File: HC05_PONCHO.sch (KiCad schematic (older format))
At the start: 15 parts

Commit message: Actualizacion de esquematico
-Esquematico graficamente completo.
-Reorganizacion por interfaces.
-Se completan los requerimientos.

Falta:
-revision externa.
-numeracion de componentes.
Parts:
- added unit 6 of Conn1
- added unit 10 of Conn1
- added unit 1 of Conn1
- added unit 11 of Conn1
- added D2: LED_ARGB, symbol LED_ARGB
- added D3: LED, symbol LED
- added J1, J2: MOUNT_HOLE, symbol CONN_01X01
- added R11, R8: 10K, symbol R
- added R2, R3, R4, R5, R6, R7: 470, symbol R
- added SW2, SW3: SW_Push, symbol SW_Push
- added U2: MOUDLE-BLUETOOTH-HC-05(34P-27X13MM), BT34P-SMD-1.5-26.9X13.0X2.2MM, symbol MOUDLE-BLUETOOTH-HC-05(34P-27X13MM)
- R1: renamed from R?; value R -> 470
- gave numbers to parts that had none: 14
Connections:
- wire segments 44 -> 92
- no-connect marks 8 -> 58
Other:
- note added: "Acelerometer interface - HMC5883L"
- note added: "Bluetooth interface HC-05"
- note added: "RGB LED Interface"
- note added: "Voltage Regulated Power Supply 9 VDC - 3.3 VDC"
- moved on the sheet: C1, C2, C3, C4, C5, Conn1N, D1, F1, J3, R1, R10, R9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

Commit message: Finalizacion de esquematico
- Componentes numerados.

falta revision externa
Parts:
- Conn1: symbol Conn_Pico -> Conn_Pico-RESCUE-HC05_PONCHO
- U2: symbol MOUDLE-BLUETOOTH-HC-05(34P-27X13MM) -> MOUDLE-BLUETOOTH-HC-05(34P-27X13MM)-RESCUE-HC05_PONCHO
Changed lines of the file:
@@
 EESchema Schematic File Version 2
+LIBS:HC05_PONCHO-rescue
 LIBS:power
 LIBS:device
@@
 $EndDescr
 $Comp
-L Conn_Pico Conn1
+L Conn_Pico-RESCUE-HC05_PONCHO Conn1
 U 14 1 58FD49CB
 P 1850 6950
@@
 $EndComp
 $Comp
-L Conn_Pico Conn1
+L Conn_Pico-RESCUE-HC05_PONCHO Conn1
 U 6 1 591BED20
 P 7150 5200
@@
 $EndComp
 $Comp
-L MOUDLE-BLUETOOTH-HC-05(34P-27X13MM) U2
+L MOUDLE-BLUETOOTH-HC-05(34P-27X13MM)-RESCUE-HC05_PONCHO U2
 U 1 1 591C3DE3
 P 5150 2400
@@
 $EndComp
 $Comp
-L Conn_Pico Conn1
+L Conn_Pico-RESCUE-HC05_PONCHO Conn1
 U 10 1 591C64F4
 P 8600 2350
@@
 $EndComp
 $Comp
-L Conn_Pico Conn1
+L Conn_Pico-RESCUE-HC05_PONCHO Conn1
 U 1 1 591C67B9
 P 2900 1750
@@
 $EndComp
 $Comp
-L Conn_Pico Conn1
+L Conn_Pico-RESCUE-HC05_PONCHO Conn1
 U 11 1 591EDA14
 P 4100 4900

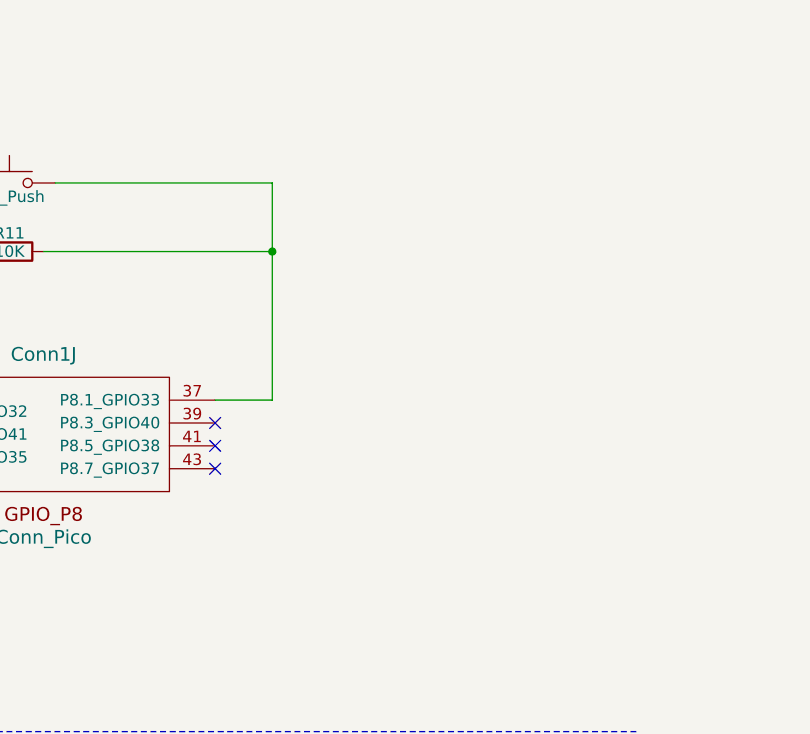
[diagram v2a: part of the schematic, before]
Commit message: Asociacion footprints - inicio  de PCB
Asociacion de footprints correspondientes para inicio de PCB
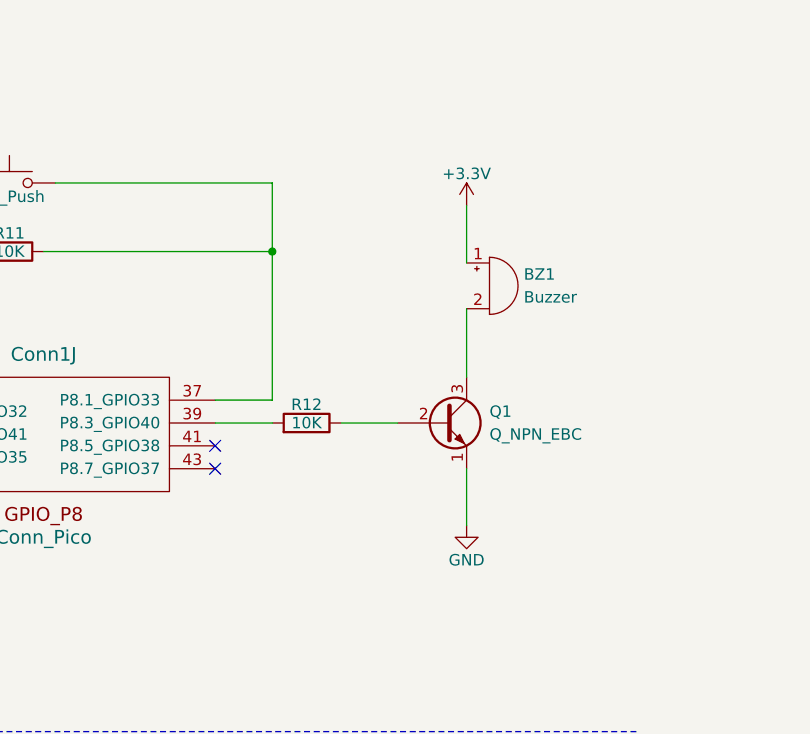
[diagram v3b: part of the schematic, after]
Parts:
- added BZ1: Buzzer, Buzzers_Beepers:MagneticBuzzer_Kingstate_KCG0601, symbol Buzzer
- added Q1: Q_NPN_EBC, TO_SOT_Packages_SMD:SOT-23, symbol Q_NPN_EBC
- added R12: 10K, Resistors_SMD:R_0603_HandSoldering, symbol R
- C1, C2: footprint (none) -> Capacitors_SMD:CP_Elec_3x5.3
- C3: footprint (none) -> Capacitors_Tantalum_SMD:CP_Tantalum_Case-A_EIA-3216-18_Hand
- C4, C5: footprint (none) -> Capacitors_SMD:C_1206_HandSoldering
- Conn1: footprint (none) -> pico_ciaa_ponchos:Conn_Pico_Ciaa
- D1, D3: footprint (none) -> LEDs:LED_1206
- D2: footprint (none) -> SML-LX0404SIUPGUSB:DIOC0404X01-4N
- F1: footprint (none) -> Fuse_Holders_and_Fuses:Fuse_SMD2920
- J1, J2: footprint (none) -> Mounting_Holes:MountingHole_3mm_Pad_Via
- J3: footprint (none) -> Connectors:BARREL_JACK
- R1, R10, R11, R2, R3, R4, R5, R6, R7, R8, R9: footprint (none) -> Resistors_SMD:R_0603_HandSoldering
- SW1: footprint (none) -> Buttons_Switches_THT:SW_NKK_G1xJP
- SW2, SW3: footprint (none) -> Buttons_Switches_THT:SW_PUSH_6mm
- U2: footprint BT34P-SMD-1.5-26.9X13.0X2.2MM -> MOUDLE-BLUETOOTH-HC-05_34P-27X13MM_:BT34P-SMD-1.5-26.9X13.0X2.2MM
- U3: footprint (none) -> HMC5883L:LPCC-16
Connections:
- net +3V3: now also BZ1.1 (-)
- net GND: now also Q1.1 (E)
- net at Conn1.39 (P8.3_GPIO40): now also R12.2
- new net: BZ1.2 (+), Q1.3 (C)
- new net: Q1.2 (B), R12.1
- no-connect marks 58 -> 57
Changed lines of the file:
@@
 F 0 "Conn1" H 1850 7300 60  0000 C CNN
 F 1 "Conn_Pico" H 1850 6500 60  0000 C CNN
-F 2 "" H 1850 6900 60  0000 C CNN
+F 2 "pico_ciaa_ponchos:Conn_Pico_Ciaa" H 1850 6900 60  0001 C CNN
 F 3 "" H 1850 6900 60  0000 C CNN
 	14   1850 6950
@@
 F 0 "J3" H 6200 7095 50  0000 C CNN
 F 1 "BARREL_JACK" H 6200 6700 50  0000 C CNN
-F 2 "" H 6200 6900 50  0001 C CNN
+F 2 "Connectors:BARREL_JACK" H 6200 6900 50  0001 C CNN
 F 3 "" H 6200 6900 50  0001 C CNN
 	1    6200 6900
@@
 F 0 "C1" H 2875 7100 50  0000 L CNN
 F 1 "10uF/16V" H 2875 6900 50  0000 L CNN
-F 2 "" H 2850 7000 50  0001 C CNN
+F 2 "Capacitors_SMD:CP_Elec_3x5.3" H 2850 7000 50  0001 C CNN
 F 3 "" H 2850 7000 50  0001 C CNN
 	1    2850 7000
@@
 F 0 "C2" H 4175 7100 50  0000 L CNN
 F 1 "100nF/25V" H 4175 6900 50  0000 L CNN
-F 2 "" H 4150 7000 50  0001 C CNN
+F 2 "Capacitors_SMD:CP_Elec_3x5.3" H 4150 7000 50  0001 C CNN
 F 3 "" H 4150 7000 50  0001 C CNN
 	1    4150 7000
@@
 F 0 "F1" V 4880 6800 50  0000 C CNN
 F 1 "Fuse" V 4725 6800 50  0000 C CNN
-F 2 "" V 4730 6800 50  0001 C CNN
+F 2 "Fuse_Holders_and_Fuses:Fuse_SMD2920" V 4730 6800 50  0001 C CNN
 F 3 "" H 4800 6800 50  0001 C CNN
 	1    4800 6800
@@
 F 0 "SW1" H 5400 6970 50  0000 C CNN
 F 1 "SW_SPDT" H 5400 6600 50  0000 C CNN
-F 2 "" H 5400 6800 50  0001 C CNN
+F 2 "Buttons_Switches_THT:SW_NKK_G1xJP" H 5400 6800 50  0001 C CNN
 F 3 "" H 5400 6800 50  0001 C CNN
 	1    5400 6800
@@
 F 0 "D1" H 1000 7300 50  0000 C CNN
 F 1 "LED" H 1000 7100 50  0000 C CNN
-F 2 "" H 1000 7200 50  0001 C CNN
+F 2 "LEDs:LED_1206" H 1000 7200 50  0001 C CNN
 F 3 "" H 1000 7200 50  0001 C CNN
 	1    1000 7200
@@
 F 0 "R1" V 1080 6750 50  0000 C CNN
 F 1 "470" V 1000 6750 50  0000 C CNN
-F 2 "" V 930 6750 50  0001 C CNN
+F 2 "Resistors_SMD:R_0603_HandSoldering" V 930 6750 50  0001 C CNN
 F 3 "" H 1000 6750 50  0001 C CNN
 	1    1000 6750
@@
 F 0 "U3" H 8800 5800 60  0000 C CNN
 F 1 "HMC5883L" H 9250 5800 60  0000 C CNN
-F 2 "" H 9050 6550 60  0000 C CNN
+F 2 "HMC5883L:LPCC-16" H 9050 6550 60  0001 C CNN
 F 3 "" H 9050 6550 60  0000 C CNN
 	1    8950 6100
@@
 F 0 "R9" V 7930 4800 50  0000 C CNN
 F 1 "2K2" V 7850 4800 50  0000 C CNN
-F 2 "" V 7780 4800 50  0001 C CNN
+F 2 "Resistors_SMD:R_0603_HandSoldering" V 7780 4800 50  0001 C CNN
 F 3 "" H 7850 4800 50  0001 C CNN
 	1    7850 4800
@@
 F 0 "R10" V 8230 4800 50  0000 C CNN
 F 1 "2K2" V 8150 4800 50  0000 C CNN
-F 2 "" V 8080 4800 50  0001 C CNN
+F 2 "Resistors_SMD:R_0603_HandSoldering" V 8080 4800 50  0001 C CNN
 F 3 "" H 8150 4800 50  0001 C CNN
 	1    8150 4800
@@
 F 0 "C4" H 9910 5720 50  0000 L CNN
 F 1 "0.22uF" H 9910 5570 50  0000 L CNN
-F 2 "" H 9900 5650 50  0001 C CNN
+F 2 "Capacitors_SMD:C_1206_HandSoldering" H 9900 5650 50  0001 C CNN
 F 3 "" H 9900 5650 50  0001 C CNN
 	1    9900 5650
@@
 F 0 "C3" H 7860 5870 50  0000 L CNN
 F 1 "4.7uF" H 7860 5720 50  0000 L CNN
-F 2 "" H 7850 5800 50  0001 C CNN
+F 2 "Capacitors_Tantalum_SMD:CP_Tantalum_Case-A_EIA-3216-18_Hand" H 7850 5800 50  0001 C CNN
 F 3 "" H 7850 5800 50  0001 C CNN
 	1    7850 5800
@@
 F 0 "C5" H 10410 5370 50  0000 L CNN
 F 1 "0.1uF" H 10410 5220 50  0000 L CNN
-F 2 "" H 10400 5300 50  0001 C CNN
+F 2 "Capacitors_SMD:C_1206_HandSoldering" H 10400 5300 50  0001 C CNN
 F 3 "" H 10400 5300 50  0001 C CNN
 	1    10400 5300
@@
 F 0 "Conn1" H 7150 5500 60  0000 C CNN
 F 1 "Conn_Pico" H 7150 4700 60  0000 C CNN
-F 2 "" H 7150 5150 60  0000 C CNN
+F 2 "pico_ciaa_ponchos:Conn_Pico_Ciaa" H 7150 5150 60  0001 C CNN
 F 3 "" H 7150 5150 60  0000 C CNN
 	6    7150 5200
@@
 F 0 "U2" H 4250 3200 50  0000 L CNN
 F 1 "MOUDLE-BLUETOOTH-HC-05(34P-27X13MM)" H 4500 3200 50  0000 L CNN
-F 2 "BT34P-SMD-1.5-26.9X13.0X2.2MM" H 5150 2400 50  0001 L CNN
+F 2 "MOUDLE-BLUETOOTH-HC-05_34P-27X13MM_:BT34P-SMD-1.5-26.9X13.0X2.2MM" H 5150 2400 50  0001 L CNN
 F 3 "" H 5150 2400 50  0001 L CNN
 F 4 "None" H 5150 2400 50  0001 L CNN "Package"
@@
 F 0 "Conn1" H 8600 2700 60  0000 C CNN
 F 1 "Conn_Pico" H 8600 1900 60  0000 C CNN
-F 2 "" H 8600 2300 60  0000 C CNN
+F 2 "pico_ciaa_ponchos:Conn_Pico_Ciaa" H 8600 2300 60  0001 C CNN
 F 3 "" H 8600 2300 60  0000 C CNN
 	10   8600 2350
@@
 F 0 "Conn1" H 2900 2100 60  0000 C CNN
 F 1 "Conn_Pico" H 2900 1300 60  0000 C CNN
-F 2 "" H 2900 1700 60  0000 C CNN
+F 2 "pico_ciaa_ponchos:Conn_Pico_Ciaa" H 2900 1700 60  0001 C CNN
 F 3 "" H 2900 1700 60  0000 C CNN
 	1    2900 1750
@@
 F 0 "D3" H 7700 3050 50  0000 C CNN
 F 1 "LED" H 7700 2850 50  0000 C CNN
-F 2 "" H 7700 2950 50  0001 C CNN
+F 2 "LEDs:LED_1206" H 7700 2950 50  0001 C CNN
 F 3 "" H 7700 2950 50  0001 C CNN
 	1    7700 2950
@@
 F 0 "R7" V 7230 2950 50  0000 C CNN
 F 1 "470" V 7150 2950 50  0000 C CNN
-F 2 "" V 7080 2950 50  0001 C CNN
+F 2 "Resistors_SMD:R_0603_HandSoldering" V 7080 2950 50  0001 C CNN
 F 3 "" H 7150 2950 50  0001 C CNN
 	1    7150 2950
@@
 F 0 "R6" V 6780 1950 50  0000 C CNN
 F 1 "470" V 6700 1950 50  0000 C CNN
-F 2 "" V 6630 1950 50  0001 C CNN
+F 2 "Resistors_SMD:R_0603_HandSoldering" V 6630 1950 50  0001 C CNN
 F 3 "" H 6700 1950 50  0001 C CNN
 	1    6700 1950
@@
 F 0 "R5" V 6780 1750 50  0000 C CNN
 F 1 "470" V 6700 1750 50  0000 C CNN
-F 2 "" V 6630 1750 50  0001 C CNN
+F 2 "Resistors_SMD:R_0603_HandSoldering" V 6630 1750 50  0001 C CNN
 F 3 "" H 6700 1750 50  0001 C CNN
 	1    6700 1750
@@
 F 0 "SW2" H 7600 1350 50  0000 L CNN
 F 1 "SW_Push" H 7550 1190 50  0000 C CNN
-F 2 "" H 7550 1450 50  0001 C CNN
+F 2 "Buttons_Switches_THT:SW_PUSH_6mm" H 7550 1450 50  0001 C CNN
 F 3 "" H 7550 1450 50  0001 C CNN
 	1    7550 1250
@@
 F 0 "R8" V 7630 1550 50  0000 C CNN
 F 1 "10K" V 7550 1550 50  0000 C CNN
-F 2 "" V 7480 1550 50  0001 C CNN
+F 2 "Resistors_SMD:R_0603_HandSoldering" V 7480 1550 50  0001 C CNN
 F 3 "" H 7550 1550 50  0001 C CNN
 	1    7550 1550
@@
 F 0 "SW3" H 8500 1350 50  0000 L CNN
 F 1 "SW_Push" H 8450 1190 50  0000 C CNN
-F 2 "" H 8450 1450 50  0001 C CNN
+F 2 "Buttons_Switches_THT:SW_PUSH_6mm" H 8450 1450 50  0001 C CNN
 F 3 "" H 8450 1450 50  0001 C CNN
 	1    8450 1250
@@
 F 0 "R11" V 8530 1550 50  0000 C CNN
 F 1 "10K" V 8450 1550 50  0000 C CNN
-F 2 "" V 8380 1550 50  0001 C CNN
+F 2 "Resistors_SMD:R_0603_HandSoldering" V 8380 1550 50  0001 C CNN
 F 3 "" H 8450 1550 50  0001 C CNN
 	1    8450 1550
@@
 F 0 "D2" H 2250 5420 50  0000 C CNN
 F 1 "LED_ARGB" H 2250 4700 50  0000 C CNN
-F 2 "" H 2250 5000 50  0001 C CNN
+F 2 "SML-LX0404SIUPGUSB:DIOC0404X01-4N" H 2250 5000 50  0001 C CNN
 F 3 "" H 2250 5000 50  0001 C CNN
 	1    2250 5050
@@
 F 0 "R3" V 2980 5050 50  0000 C CNN
 F 1 "470" V 2900 5050 50  0000 C CNN
-F 2 "" V 2830 5050 50  0001 C CNN
+F 2 "Resistors_SMD:R_0603_HandSoldering" V 2830 5050 50  0001 C CNN
 F 3 "" H 2900 5050 50  0001 C CNN
 	1    2900 5050
@@
 F 0 "R2" V 2980 4850 50  0000 C CNN
 F 1 "470" V 2900 4850 50  0000 C CNN
-F 2 "" V 2830 4850 50  0001 C CNN
+F 2 "Resistors_SMD:R_0603_HandSoldering" V 2830 4850 50  0001 C CNN
 F 3 "" H 2900 4850 50  0001 C CNN
 	1    2900 4850
@@
 F 0 "R4" V 2980 5250 50  0000 C CNN
 F 1 "470" V 2900 5250 50  0000 C CNN
-F 2 "" V 2830 5250 50  0001 C CNN
+F 2 "Resistors_SMD:R_0603_HandSoldering" V 2830 5250 50  0001 C CNN
 F 3 "" H 2900 5250 50  0001 C CNN
 	1    2900 5250
@@
 F 0 "Conn1" H 4100 5500 60  0000 C CNN
 F 1 "Conn_Pico" H 4100 4150 60  0000 C CNN
-F 2 "" H 4100 4850 60  0000 C CNN
+F 2 "pico_ciaa_ponchos:Conn_Pico_Ciaa" H 4100 4850 60  0001 C CNN
 F 3 "" H 4100 4850 60  0000 C CNN
 	11   4100 4900
@@
 F 0 "J1" H 1000 3500 50  0000 C CNN
 F 1 "MOUNT_HOLE" V 1100 3400 50  0000 C CNN
-F 2 "" H 1000 3400 50  0001 C CNN
+F 2 "Mounting_Holes:MountingHole_3mm_Pad_Via" H 1000 3400 50  0001 C CNN
 F 3 "" H 1000 3400 50  0001 C CNN
 	1    1000 3400
@@
 F 0 "J2" H 1750 3500 50  0000 C CNN
 F 1 "MOUNT_HOLE" V 1850 3400 50  0000 C CNN
-F 2 "" H 1750 3400 50  0001 C CNN
+F 2 "Mounting_Holes:MountingHole_3mm_Pad_Via" H 1750 3400 50  0001 C CNN
 F 3 "" H 1750 3400 50  0001 C CNN
 	1    1750 3400
 	0    1    1    0
 $EndComp
-NoConn ~ 9350 2300
 NoConn ~ 9350 2400
 NoConn ~ 9350 2500
@@
 	1    0    0    -1
 $EndComp
+$Comp
+L Buzzer BZ1
+U 1 1 59349DF9
+P 10550 1700
+F 0 "BZ1" H 10700 1750 50  0000 L CNN
+F 1 "Buzzer" H 10700 1650 50  0000 L CNN
+F 2 "Buzzers_Beepers:MagneticBuzzer_Kingstate_KCG0601" V 10525 1800 50  0001 C CNN
+F 3 "" V 10525 1800 50  0001 C CNN
+	1    10550 1700
+	1    0    0    -1
+$EndComp
+$Comp
+L Q_NPN_EBC Q1
+U 1 1 59349EF9
+P 10350 2300
+F 0 "Q1" H 10550 2350 50  0000 L CNN
+F 1 "Q_NPN_EBC" H 10550 2250 50  0000 L CNN
+F 2 "TO_SOT_Packages_SMD:SOT-23" H 10550 2400 50  0001 C CNN
+F 3 "" H 10350 2300 50  0001 C CNN
+	1    10350 2300
+	1    0    0    -1
+$EndComp
+$Comp
+L R R12
+U 1 1 5934A562
+P 9750 2300
+F 0 "R12" V 9830 2300 50  0000 C CNN
+F 1 "10K" V 9750 2300 50  0000 C CNN
+F 2 "Resistors_SMD:R_0603_HandSoldering" V 9680 2300 50  0001 C CNN
+F 3 "" H 9750 2300 50  0001 C CNN
+	1    9750 2300
+	0    1    -1   0
+$EndComp
+$Comp
+L +3.3V #PWR018
+U 1 1 5934B8B9
+P 10450 1350
+F 0 "#PWR018" H 10450 1200 50  0001 C CNN
+F 1 "+3.3V" H 10450 1490 50  0000 C CNN
+F 2 "" H 10450 1350 50  0001 C CNN
+F 3 "" H 10450 1350 50  0001 C CNN
+	1    10450 1350
+	1    0    0    -1
+$EndComp
+$Comp
+L GND #PWR019
+U 1 1 5934B933
+P 10450 2750
+F 0 "#PWR019" H 10450 2500 50  0001 C CNN
+F 1 "GND" H 10450 2600 50  0000 C CNN
+F 2 "" H 10450 2750 50  0001 C CNN
+F 3 "" H 10450 2750 50  0001 C CNN
+	1    10450 2750
+	1    0    0    -1
+$EndComp
+Wire Wire Line
+	9350 2300 9600 2300
+Wire Wire Line
+	9900 2300 10150 2300
+Wire Wire Line
+	10450 1600 10450 1350
+Wire Wire Line
+	10450 2100 10450 1800
+Wire Wire Line
+	10450 2750 10450 2500
 $EndSCHEMATC

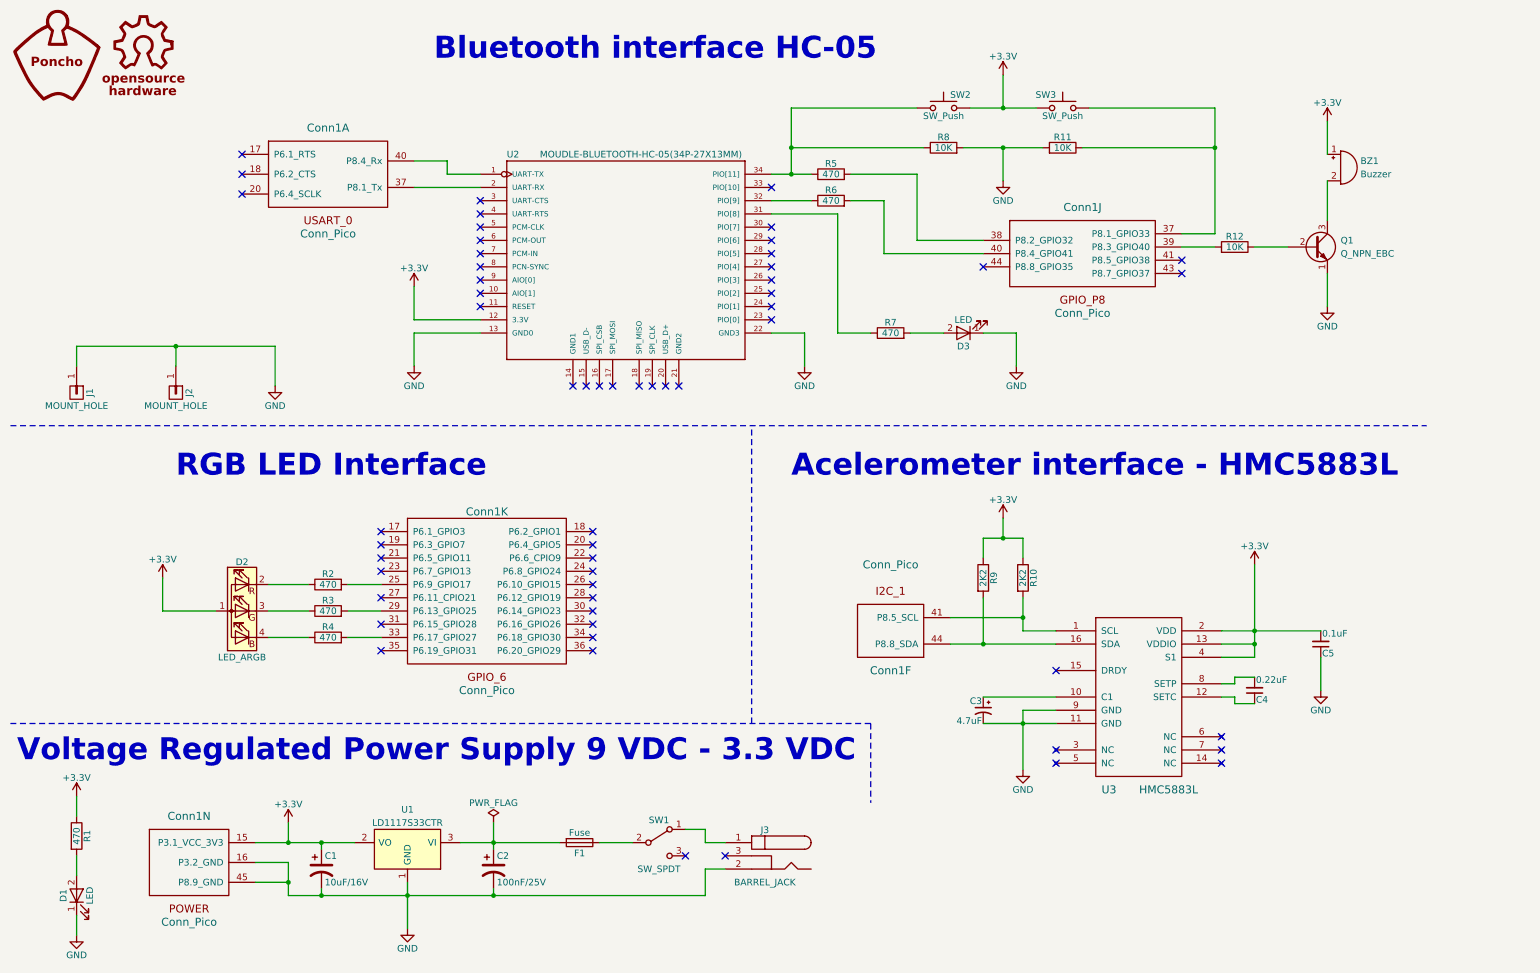
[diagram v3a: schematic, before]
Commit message: Esquematico V1.1
Correccion parcial de las observaciones realizadas por el revisor, se reflejan el archivo de revision ubicado en la carpeta doc
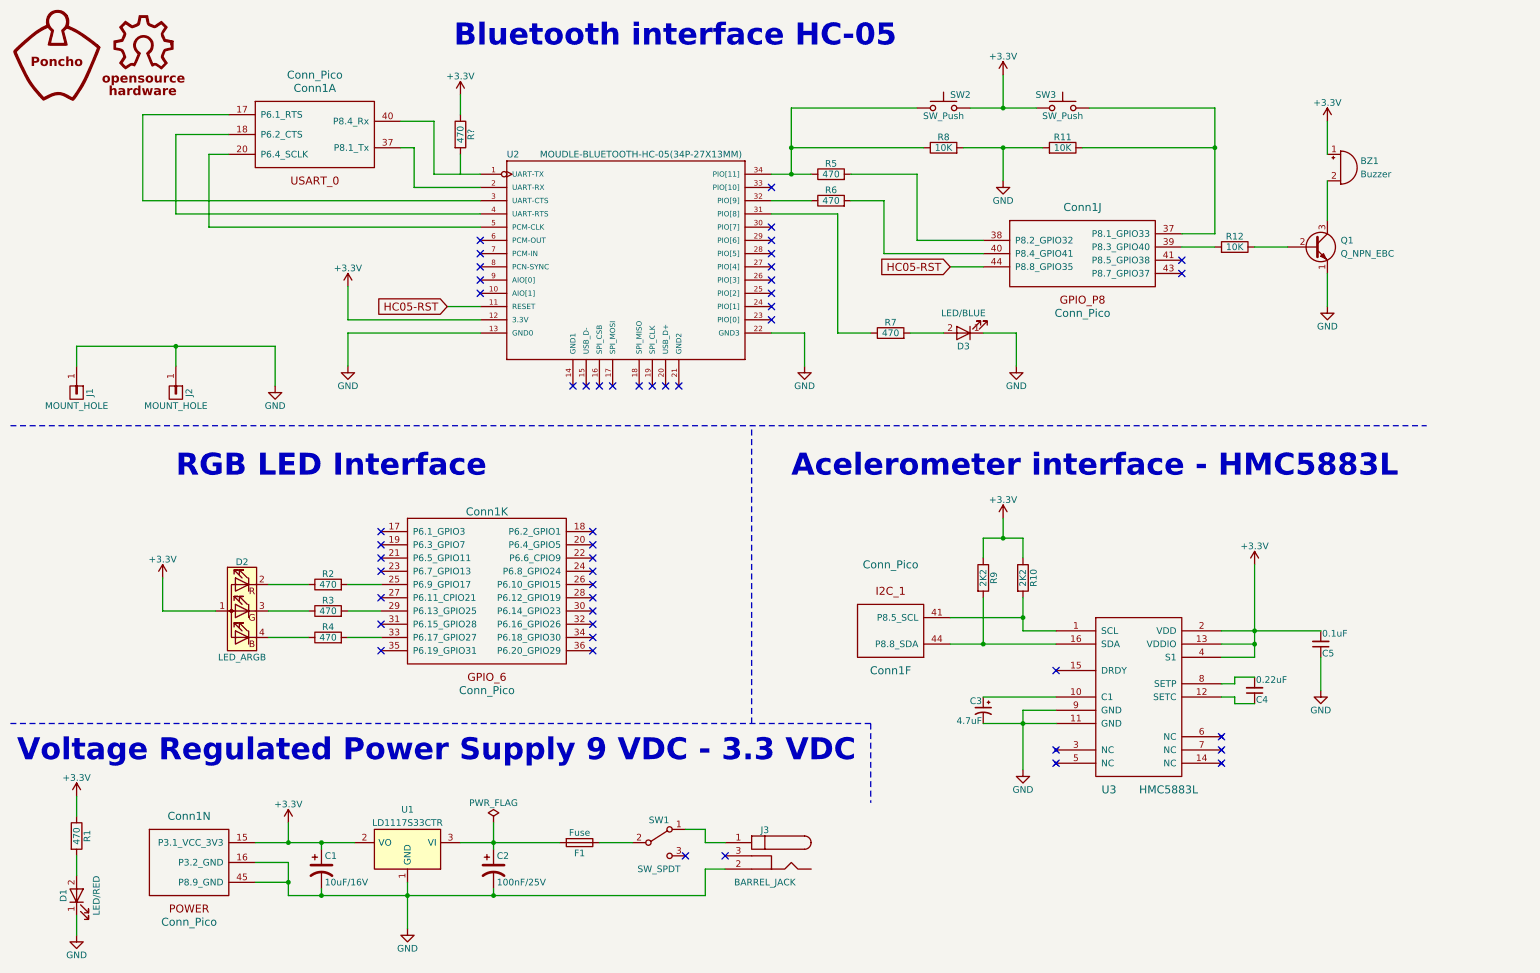
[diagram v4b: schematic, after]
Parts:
- added R?: 470, Resistors_SMD:R_0603_HandSoldering, symbol R
- D1: value LED -> LED/RED
- D3: value LED -> LED/BLUE
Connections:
- net +3V3: now also R?.1
- net HC05-RST: now reaches U2.11 (RESET)
- net HC05-RST: now also Conn1.44 (P8.8_GPIO35)
- net at U2.3 (UART-CTS): now also Conn1.17 (P6.1_RTS)
- net at U2.4 (UART-RTS): now also Conn1.18 (P6.2_CTS)
- net at U2.5 (PCM-CLK): now also Conn1.20 (P6.4_SCLK)
- no-connect marks 57 -> 49
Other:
- moved on the sheet: Conn1A
